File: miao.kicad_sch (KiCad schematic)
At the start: 17 parts, among them J1 USB_C_Receptacle_USB2.0, SW1 BOOT, SW2 RESET, U2 USBLC6-2SC6, U3 xiao_drop-in_gpio_usb_no_cuto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

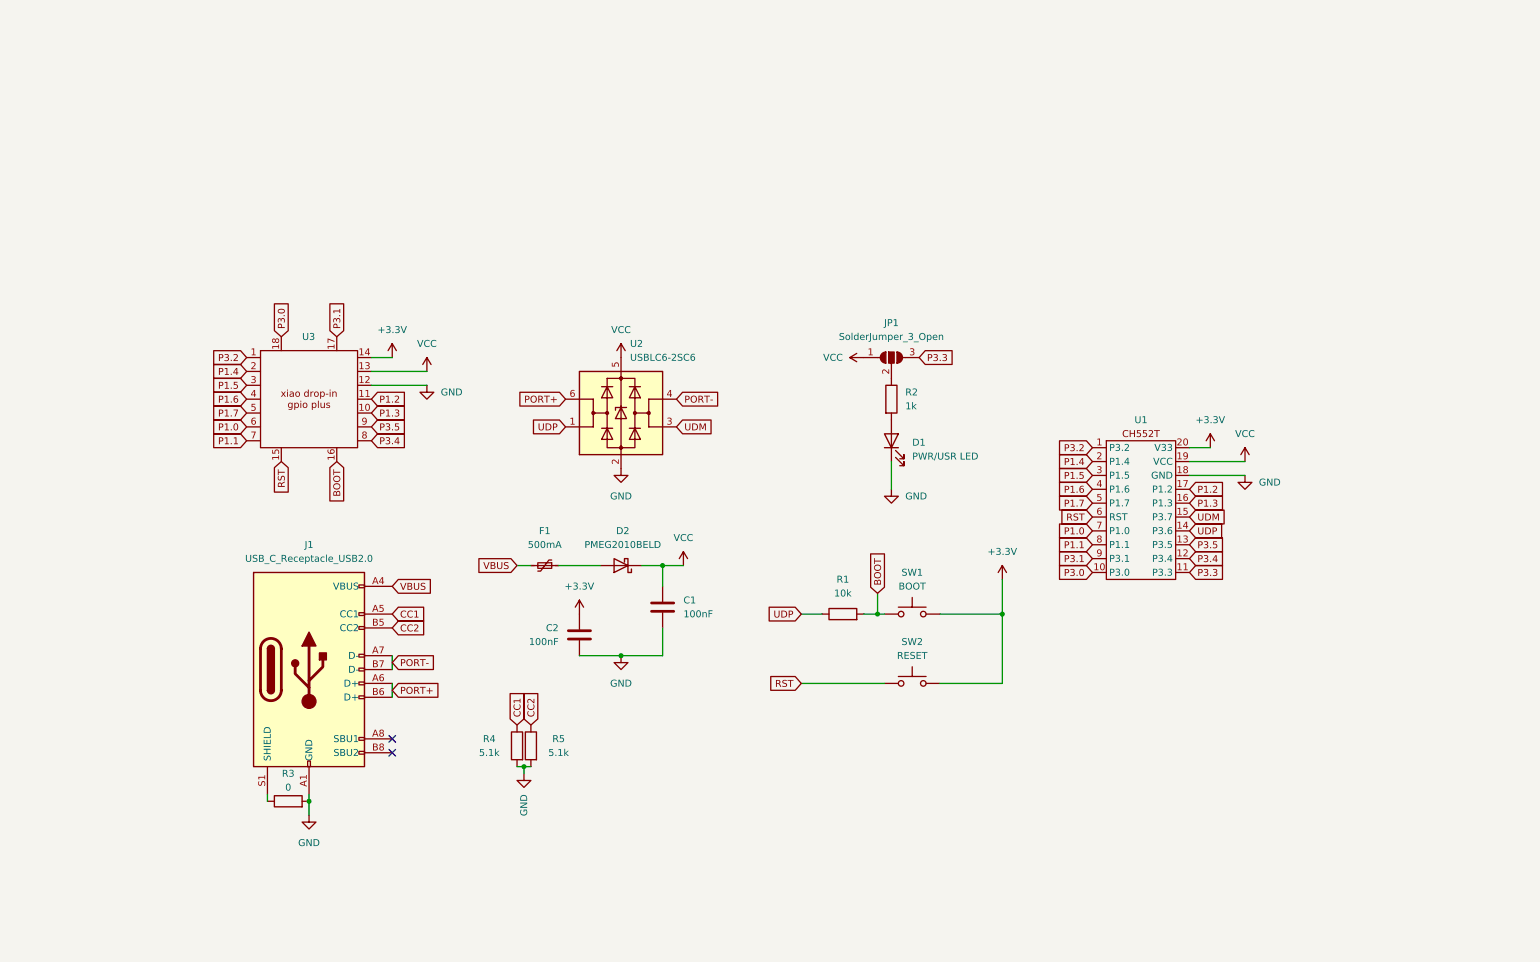
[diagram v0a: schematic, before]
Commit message: hopefully fix pin-out errors to add more compat
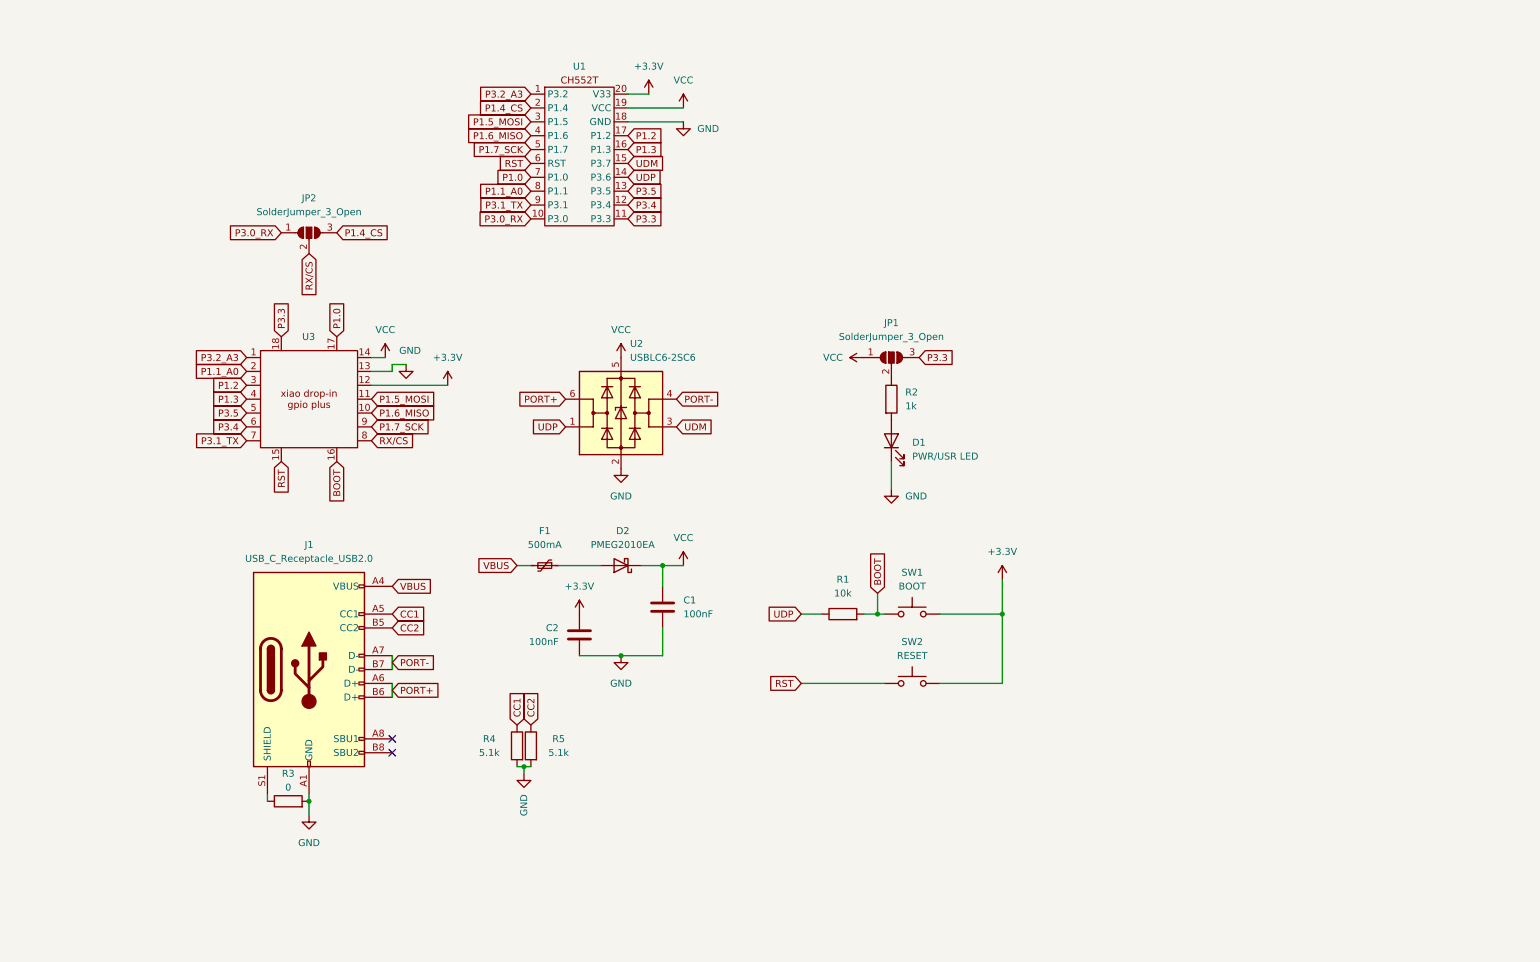
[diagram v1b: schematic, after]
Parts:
- added JP2: SolderJumper_3_Open, BeiBob:SolderJumper-3_P1.3mm_Open_RoundedPad1.0x1.5mm_NumberLabels, symbol Jumper:SolderJumper_3_Open
- D2: value PMEG2010BELD -> PMEG2010EA
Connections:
- net +3.3V: now also U3.12; no longer U3.14
- net GND: now also U3.13; no longer U3.12
- net P1.0: now also U3.17; no longer U3.6
- net P1.2: now also U3.3; no longer U3.11
- net P1.3: now also U3.4; no longer U3.10
- net P3.3: now also U3.18
- net P3.4: now also U3.6; no longer U3.8
- net P3.5: now also U3.5; no longer U3.9
- net VCC: now also U3.14; no longer U3.13
- net P1.1 renamed P1.1_A0
- net P1.1_A0: now also U3.2; no longer U3.7
- net P1.4 renamed P1.4_CS
- net P1.4_CS: now also JP2.3 (B); no longer U3.2
- net P1.5 renamed P1.5_MOSI
- net P1.5_MOSI: now also U3.11; no longer U3.3
- net P1.6 renamed P1.6_MISO
- net P1.6_MISO: now also U3.10; no longer U3.4
- net P1.7 renamed P1.7_SCK
- net P1.7_SCK: now also U3.9; no longer U3.5
- net P3.0 renamed P3.0_RX
- net P3.0_RX: now also JP2.1 (A); no longer U3.18
- net P3.1 renamed P3.1_TX
- net P3.1_TX: now also U3.7; no longer U3.17
- net P3.2 renamed P3.2_A3
- new net RX/CS: JP2.2 (C), U3.8
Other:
- moved on the sheet: U1

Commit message: update README, clean-up schematic
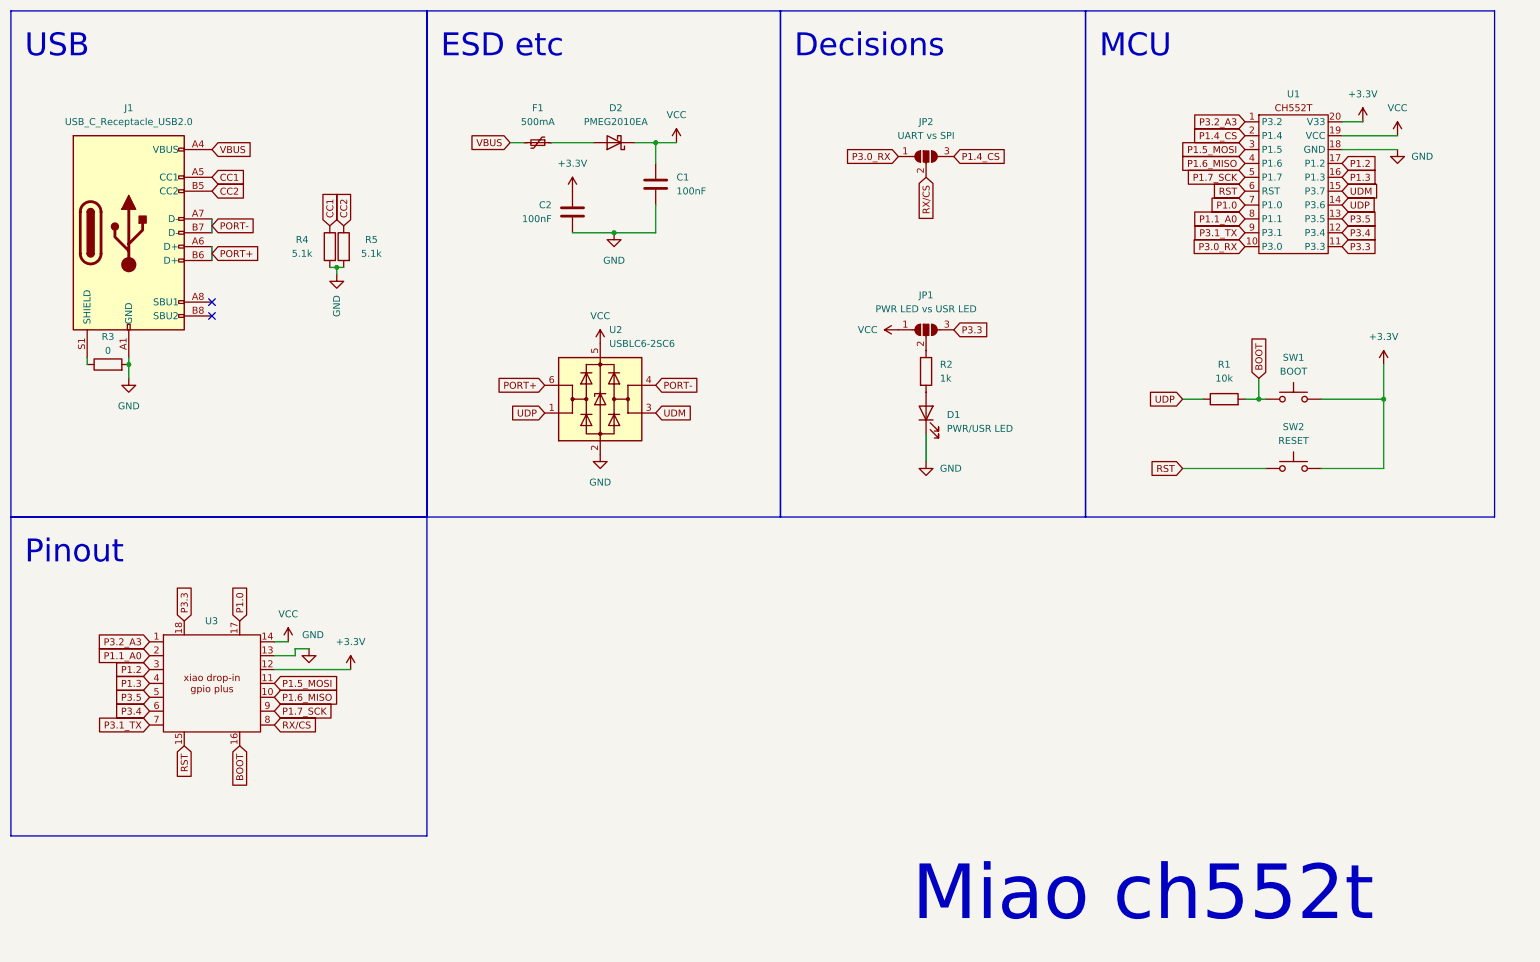
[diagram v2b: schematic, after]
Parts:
- JP1: value SolderJumper_3_Open -> PWR LED vs USR LED
- JP2: value SolderJumper_3_Open -> UART vs SPI
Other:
- note added: "Decisions"
- note added: "ESD etc"
- note added: "MCU"
- note added: "Miao ch552t"
- note added: "Pinout"
- note added: "USB"
- moved on the sheet: C1, C2, D1, D2, F1, J1, JP1, JP2, R1, R2, R3, R4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
